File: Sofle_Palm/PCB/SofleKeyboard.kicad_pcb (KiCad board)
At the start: 2 copper layers, 143.3 x 111.8 mm, 100 parts, among them J1 LED, J2 4PIN, J3 OLED, J4 key leds, J5 backlight sel, J6 indicator bypass, J7 Conn_01x05_Female, P1 i2c_pin, P2 i2c_pin, SW1 SW_PUSH-MX_W_LED, SW10 SW_PUSH-MX_W_LED, SW11 SW_PUSH-MX_W_LED, SW12 SW_PUSH-MX_W_LED, SW13 SW_PUSH-MX_W_LED, SW14 SW_PUSH-MX_W_LED, SW15 SW_PUSH-MX_W_LED, SW16 SW_PUSH-MX_W_LED, SW17 SW_PUSH-MX_W_LED, SW18 SW_PUSH-MX_W_LED, SW19 SW_PUSH-MX_W_LED, SW2 SW_PUSH-MX_W_LED, SW20 SW_PUSH-MX_W_LED, SW21 SW_PUSH-MX_W_LED, SW22 SW_PUSH-MX_W_LED, SW23 SW_PUSH-MX_W_LED, SW24 SW_PUSH-MX_W_LED, SW25 Rotary_Encoder_Switch, SW26 SW_PUSH-MX_W_LED, SW27 SW_PUSH-MX_W_LED, SW28 SW_PUSH-MX_W_LED, SW29 SW_PUSH-MX_W_LED, SW3 SW_PUSH-MX_W_LED, SW30 SW_PUSH-MX_W_LED, SW4 SW_PUSH-MX_W_LED, SW44 EVQWGD001, SW5 SW_PUSH-MX_W_LED, SW6 SW_PUSH-MX_W_LED, SW7 SW_PUSH-MX_W_LED, SW8 SW_PUSH-MX_W_LED, SW9 SW_PUSH-MX_W_LED, U1 ProMicro

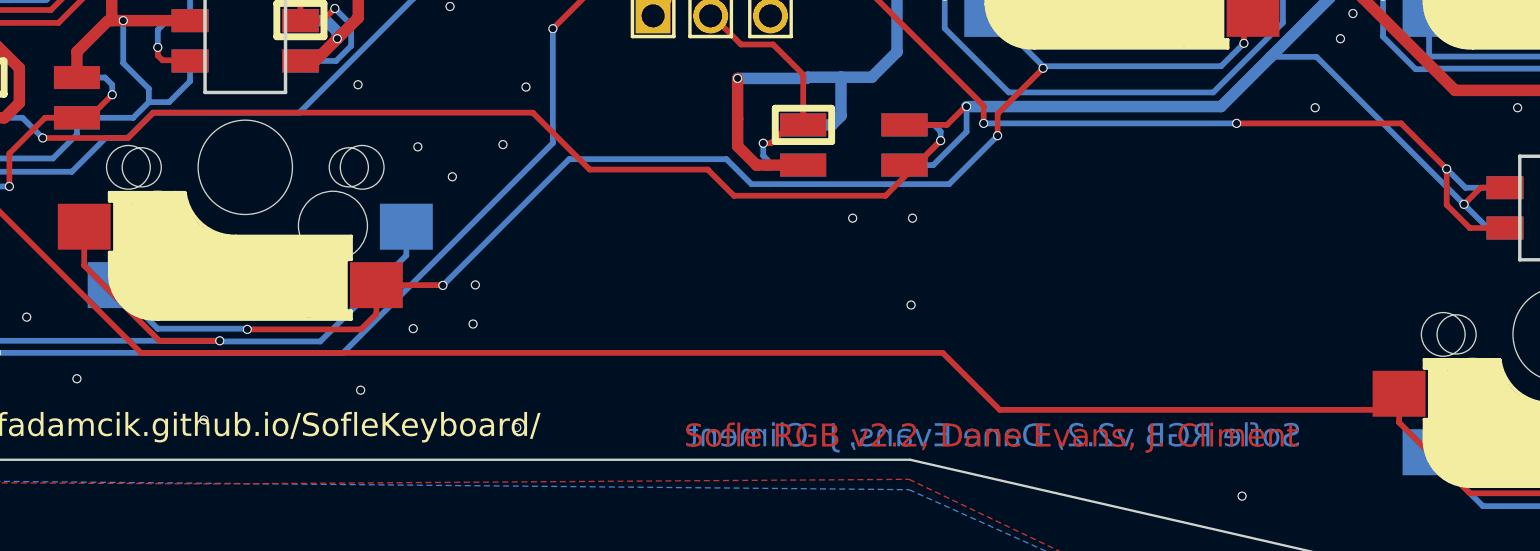
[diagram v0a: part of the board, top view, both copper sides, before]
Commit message: Updated libraries for local . Reroute path of palm area.
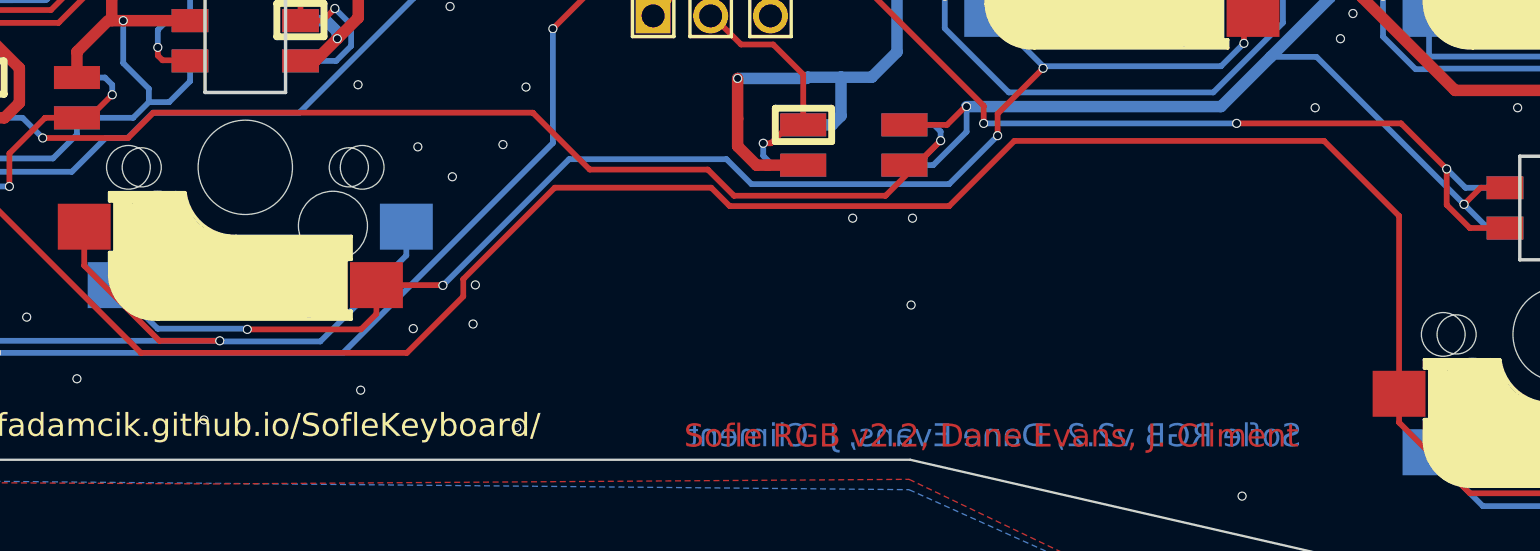
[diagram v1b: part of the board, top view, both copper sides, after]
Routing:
- net Net-(D30-Pad2): track 106.7 -> 120.3 mm

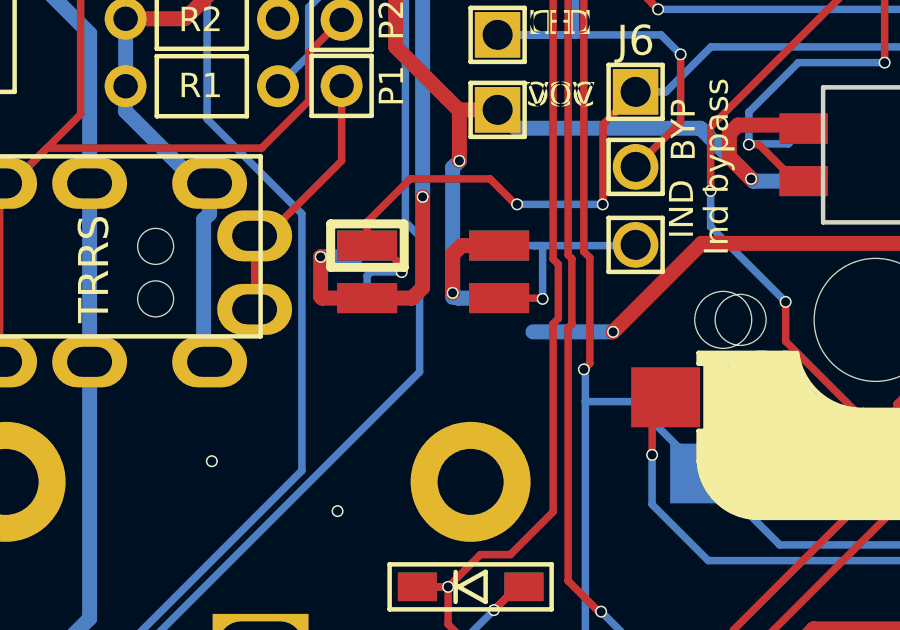
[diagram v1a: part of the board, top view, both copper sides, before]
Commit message: Added new key for Case TOP.
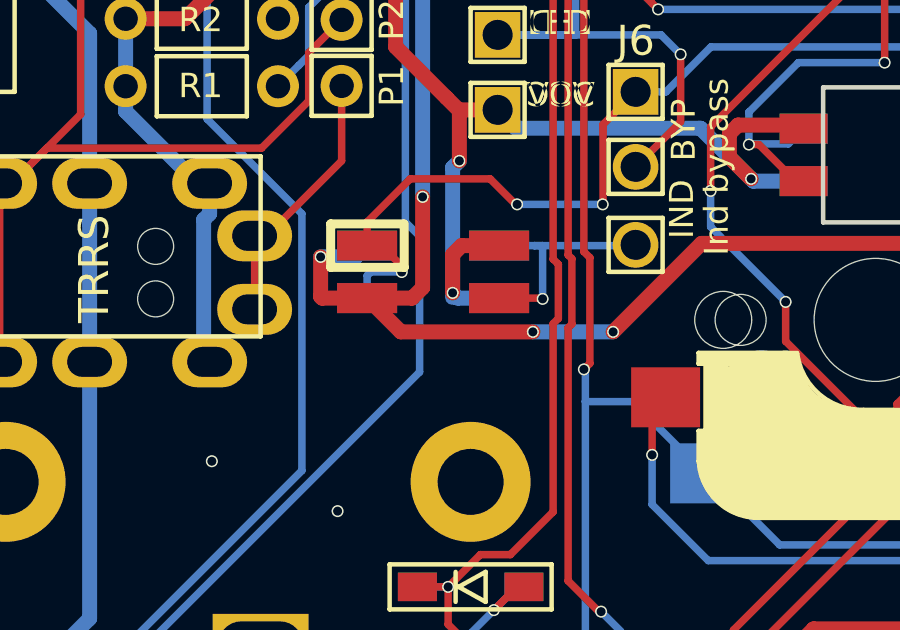
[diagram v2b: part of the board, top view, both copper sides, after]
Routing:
- net GND: track 1034.9 -> 1040.8 mm, vias 230 -> 231

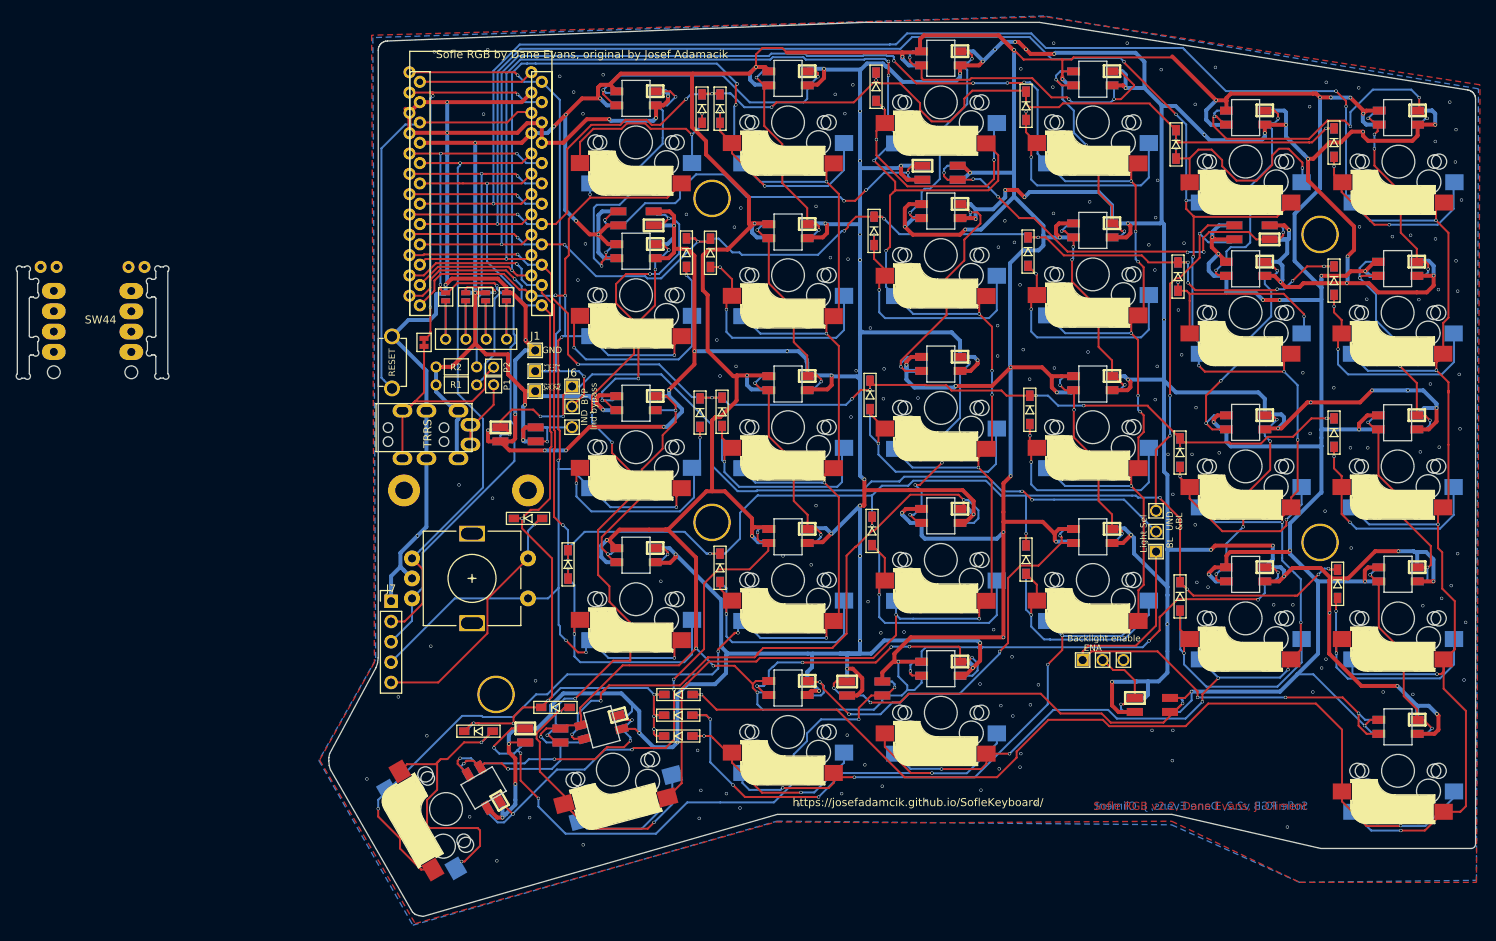
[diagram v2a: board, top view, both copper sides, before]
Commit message: Routed 5-pin connector to the palm area for the roller encoder.
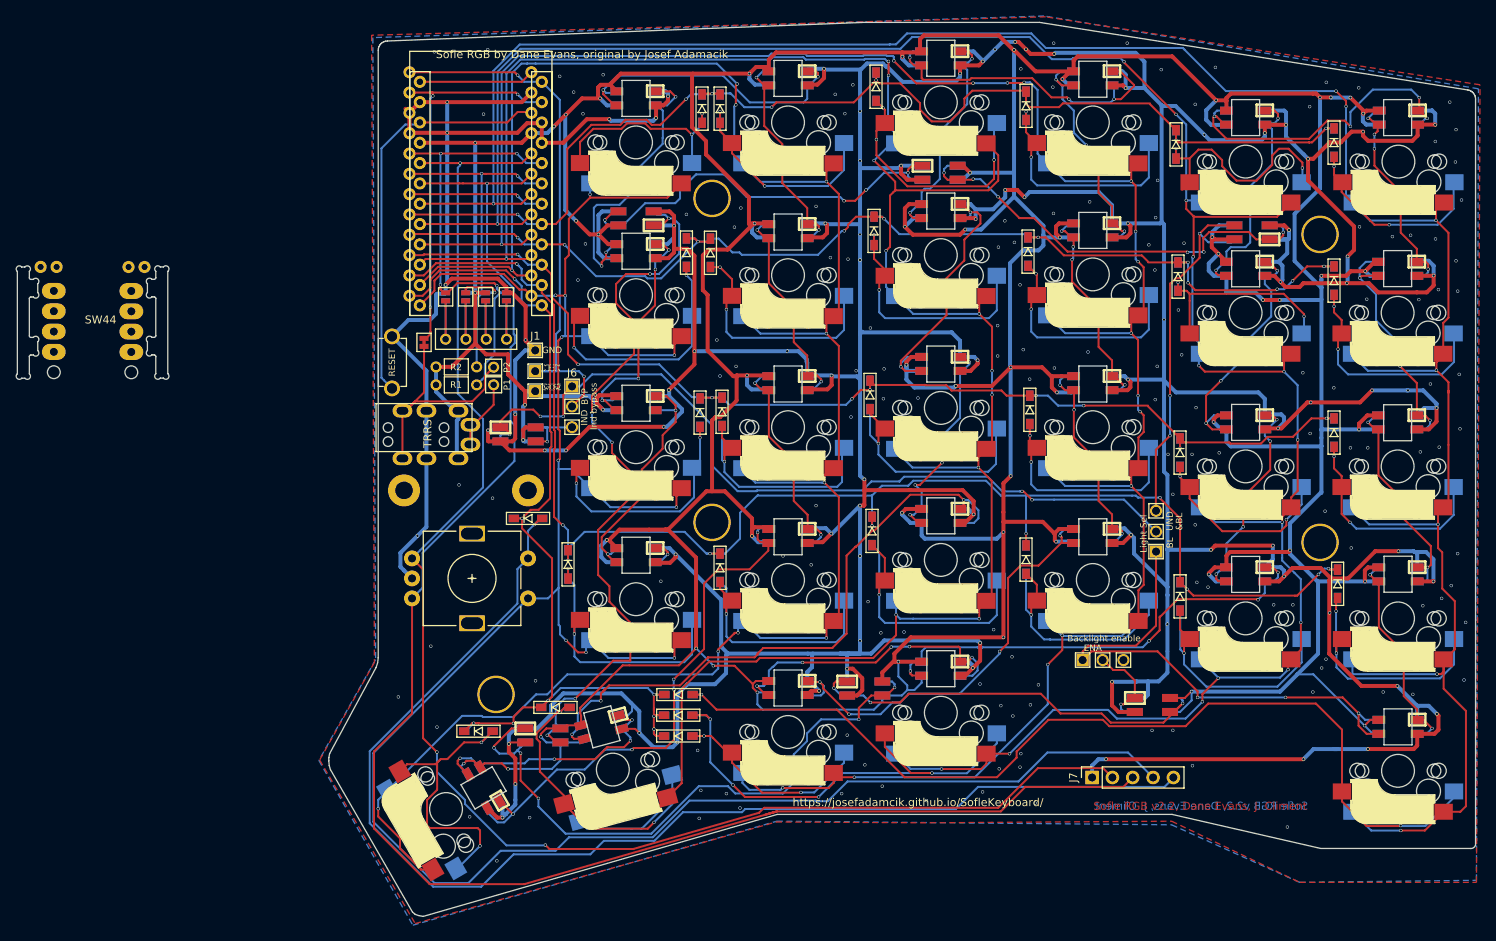
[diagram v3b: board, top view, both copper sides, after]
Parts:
- J7: value Conn_01x05_Female -> Pin socket; footprint Connector_PinHeader_2.54mm:PinHeader_1x05_P2.54mm_Vertical -> Connector_PinSocket_2.54mm:PinSocket_1x05_P2.54mm_Vertical
- moved J7 90.4 mm to (177.5, 129.4), turned to 90 degrees
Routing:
- net ENCB: track 80.0 -> 207.6 mm
- net SW25B: track 33.2 -> 157.9 mm
- net SW25A: track 173.7 -> 298.0 mm
- net ENCA: track 80.0 -> 189.1 mm, vias 1 -> 3
- net GND: track 1040.8 -> 1080.7 mm
- net Net-(D34-Pad1): track 77.9 -> 78.6 mm
- net VCC: track 926.0 -> 925.4 mm

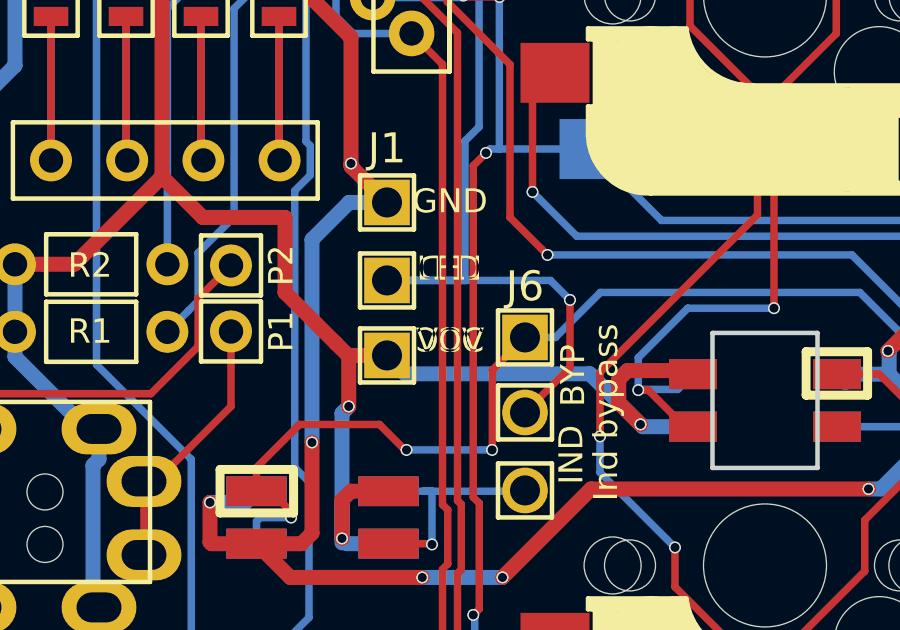
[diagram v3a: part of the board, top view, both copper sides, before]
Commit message: Completed Soufflé board with palm key. Missing the roller encoder.
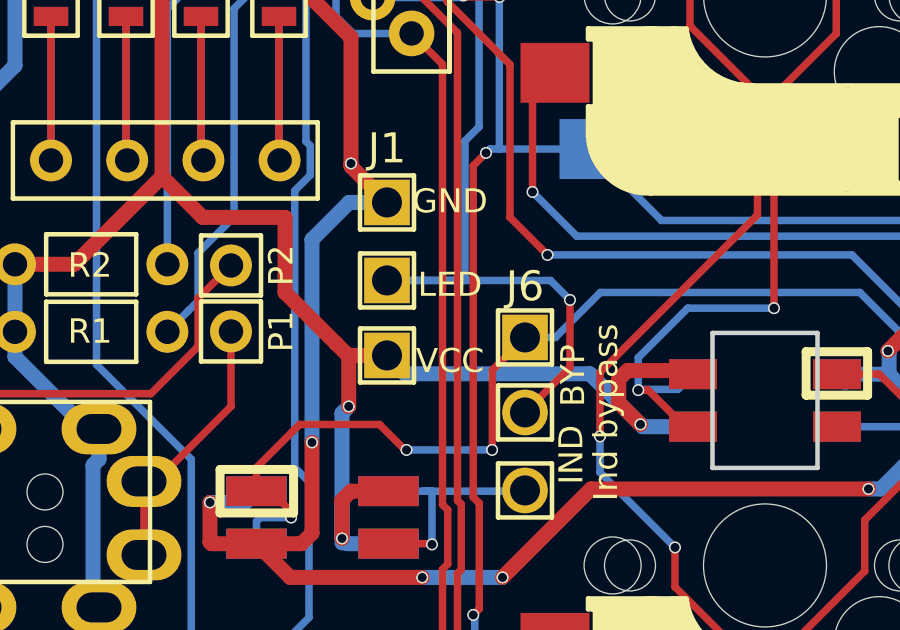
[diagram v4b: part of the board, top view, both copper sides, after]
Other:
- board text removed: "LED"
- board text removed: "VCC"
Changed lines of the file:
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@@
   (general
     (thickness 1.6)
-    (drawings 369)
+    (drawings 367)
     (tracks 3778)
     (zones 0)
@@
       (effects (font (size 1 1) (thickness 0.15)))
     )
-    (fp_text user %R (at 0 5.08) (layer F.Fab)
-      (effects (font (size 1 1) (thickness 0.15)))
-    )
     (fp_line (start -1.27 -1.27) (end 0.635 -1.27) (layer F.Fab) (width 0.1))
     (fp_line (start 0.635 -1.27) (end 1.27 -0.635) (layer F.Fab) (width 0.1))
@@
     (fp_line (start 1.75 11.9) (end -1.8 11.9) (layer F.CrtYd) (width 0.05))
     (fp_line (start -1.8 11.9) (end -1.8 -1.8) (layer F.CrtYd) (width 0.05))
+    (fp_text user %R (at 0 5.08) (layer F.Fab)
+      (effects (font (size 1 1) (thickness 0.15)))
+    )
     (pad 5 thru_hole oval (at 0 10.16 90) (size 1.7 1.7) (drill 1) (layers *.Cu *.Mask)
       (net 53 SW25B))
@@
       (effects (font (size 0.8 0.8) (thickness 0.15)) (justify mirror))
     )
-    (fp_text user LED (at -2.1 2.9 180) (layer F.SilkS)
-      (effects (font (size 0.8 0.8) (thickness 0.15)) (justify mirror))
+    (fp_text user LED (at -2.1 2.36 180) (layer F.SilkS)
+      (effects (font (size 0.8 0.8) (thickness 0.15)))
     )
     (fp_text user GND (at -2.1 5.1 180) (layer B.SilkS)
       (effects (font (size 0.8 0.8) (thickness 0.15)) (justify mirror))
     )
-    (fp_text user VCC (at -2.2 0.1 180) (layer B.SilkS)
+    (fp_text user VCC (at -2.2 -0.18 180) (layer B.SilkS)
       (effects (font (size 0.8 0.8) (thickness 0.15)) (justify mirror))
     )
-    (fp_text user VCC (at -2.1 0.5 180) (layer F.SilkS)
-      (effects (font (size 0.8 0.8) (thickness 0.15)) (justify mirror))
+    (fp_text user VCC (at -2.1 -0.18 180) (layer F.SilkS)
+      (effects (font (size 0.8 0.8) (thickness 0.15)))
     )
     (fp_text user J1 (at 0 6.9 180) (layer B.SilkS)
@@
     (effects (font (size 0.8 0.8) (thickness 0.15)))
   )
-  (gr_text VCC (at 110 80.6) (layer F.SilkS)
-    (effects (font (size 0.8 0.8) (thickness 0.15)))
-  )
-  (gr_text LED (at 109.96 78.2) (layer F.SilkS)
-    (effects (font (size 0.8 0.8) (thickness 0.15)))
-  )
